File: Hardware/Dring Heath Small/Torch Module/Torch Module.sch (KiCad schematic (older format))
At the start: 32 parts, among them J1 Torch, J10 Module conn, J2 Module3, J3 Conn_01x18_Male, J4 Limit, J6 Motor, J7 Module1, J8 Torch, J9 2.54 pin, K1 G6E, Q1 AO3400A, U1 ULN2002

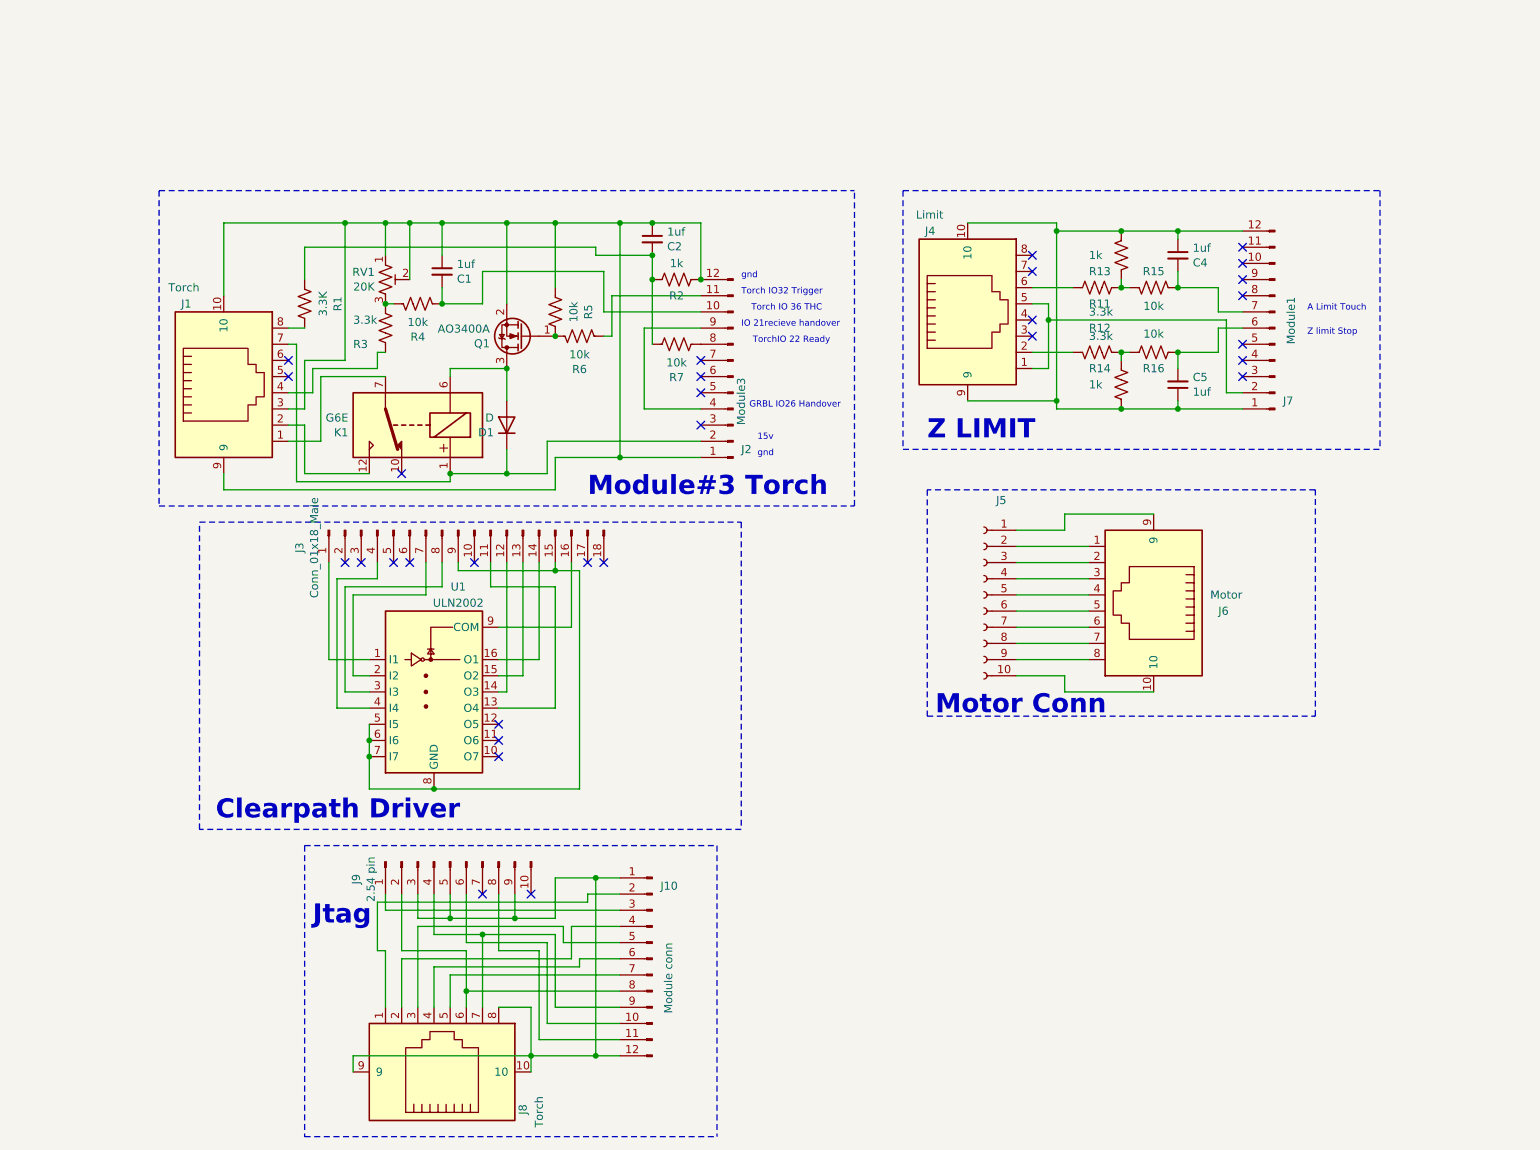
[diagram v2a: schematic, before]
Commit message: Made workspace for vscode
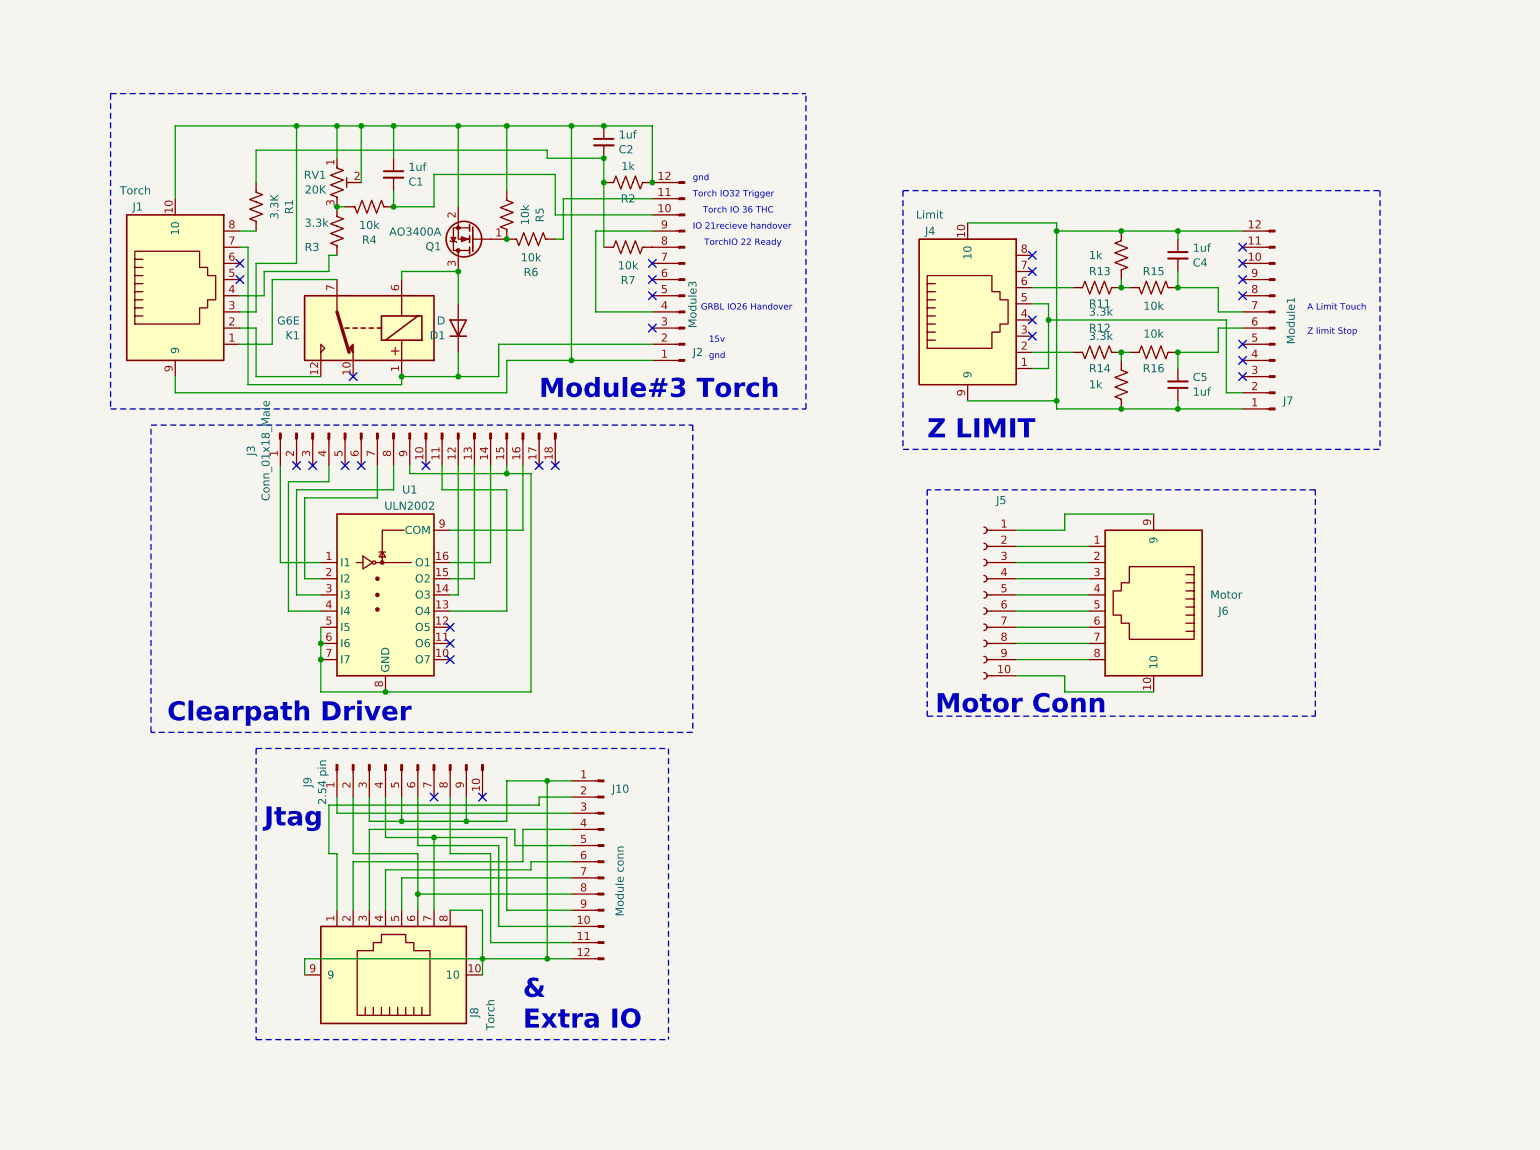
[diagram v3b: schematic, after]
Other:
- note added: "&\nExtra IO"
- moved on the sheet: C1, C2, D1, J1, J10, J2, J3, J8, J9, K1, Q1, R1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

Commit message: Added mosfet motor driver
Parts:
- added J11: Conn_01x18_Male, Modules:ClearpathDriver, symbol Connector:Conn_01x18_Male
- added Q2, Q3, Q4, Q5: IRLML2402, Package_TO_SOT_SMD:SOT-23, symbol Device:Q_NMOS_GDS
- added R10, R18, R20, R8: 200, Resistor_SMD:R_0603_1608Metric_Pad0.98x0.95mm_HandSolder, symbol Device:R_US
- added R17, R19, R21, R9: 10k, Resistor_SMD:R_0603_1608Metric_Pad0.98x0.95mm_HandSolder, symbol Device:R_US
- Q1: value AO3400A -> IRLML2402
- R6: value 10k -> 200
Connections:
- new net: J11.1 (Pin_1), R8.1
- new net: J11.11 (Pin_11), Q5.2 (D)
- new net: J11.12 (Pin_12), Q3.2 (D)
- new net: J11.13 (Pin_13), Q4.2 (D)
- new net: J11.14 (Pin_14), Q2.2 (D)
- new net: J11.15 (Pin_15), J11.9 (Pin_9), Q2.3 (S), Q3.3 (S), Q4.3 (S), Q5.3 (S), R17.2, R19.2, R21.2, R9.2
- new net: J11.4 (Pin_4), R20.1
- new net: J11.7 (Pin_7), R18.1
- new net: J11.8 (Pin_8), R10.1
- new net: Q2.1 (G), R8.2, R9.1
- new net: Q4.1 (G), R18.2, R19.1
- new net: Q3.1 (G), R10.2, R17.1
- new net: Q5.1 (G), R20.2, R21.1
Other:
- note added: "Mosfet Driver"
- moved on the sheet: C1, C2, C4, C5, D1, J1, J10, J2, J3, J4, J5, J6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

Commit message: Changed voltage divider for THC input
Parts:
- C1: value 1uf -> 22nf
- R3: value 3.3k -> 1k
- RV1: value 20K -> 2K
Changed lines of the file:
@@
 AR Path="/61469ABE/61A6725D" Ref="C?"  Part="1"
 F 0 "C1" H 3758 1254 50  0000 R CNN
-F 1 "1uf" H 3758 1345 50  0000 R CNN
+F 1 "22nf" H 3758 1345 50  0000 R CNN
 F 2 "Capacitor_SMD:C_0603_1608Metric_Pad1.08x0.95mm_HandSolder" H 3850 1300 50  0001 C CNN
 F 3 "~" H 3850 1300 50  0001 C CNN
@@
 AR Path="/61469ABE/61A6724B" Ref="R?"  Part="1"
 F 0 "R3" H 3700 1750 50  0000 R CNN
-F 1 "3.3k" H 3700 1600 50  0000 R CNN
+F 1 "1k" H 3700 1600 50  0000 R CNN
 F 2 "Resistor_SMD:R_0603_1608Metric_Pad0.98x0.95mm_HandSolder" V 3540 1640 50  0001 C CNN
 F 3 "~" H 3500 1650 50  0001 C CNN
@@
 P 3500 1350
 F 0 "RV1" H 3433 1396 50  0000 R CNN
-F 1 "20K" H 3433 1305 50  0000 R CNN
+F 1 "2K" H 3433 1305 50  0000 R CNN
 F 2 "Potentiometer_THT:Potentiometer_Bourns_3339S_Horizontal" H 3500 1350 50  0001 C CNN
 F 3 "~" H 3500 1350 50  0001 C CNN

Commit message: put protection resistors on JTAG module
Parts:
- added R22, R23, R24, R25, R26, R27, R28, R29: 200, Resistor_SMD:R_0603_1608Metric_Pad0.98x0.95mm_HandSolder, symbol Device:R_US
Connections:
- net at J10.10 (Pin_10): now also R28.1; no longer J9.6 (Pin_6)
- net at J10.11 (Pin_11): now also R29.1; no longer J9.8 (Pin_8)
- net at J10.4 (Pin_4): now also R22.1; no longer J8.2
- net at J10.5 (Pin_5): now also R23.1; no longer J8.3
- net at J10.6 (Pin_6): now also R24.1; no longer J8.4
- net at J10.7 (Pin_7): now also R25.1; no longer J8.5
- net at J8.6, J9.2 (Pin_2): now also R26.2; no longer J10.8 (Pin_8)
- net at J8.7, J9.4 (Pin_4): now also R27.2; no longer J10.9 (Pin_9)
- new net: J10.8 (Pin_8), R26.1
- new net: J10.9 (Pin_9), R27.1
- new net: J9.6 (Pin_6), R28.2
- new net: J9.8 (Pin_8), R29.2
- new net: J8.2, R22.2
- new net: J8.3, R23.2
- new net: J8.4, R24.2
- new net: J8.5, R25.2
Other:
- moved on the sheet: J10
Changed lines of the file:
@@
 	3500 5150 3500 5250
 Wire Wire Line
-	3500 5250 4950 5250
+	3500 5250 5150 5250
 Wire Wire Line
 	4600 5350 4600 5450
 Wire Wire Line
-	4600 5450 4950 5450
-Wire Wire Line
 	4550 5300 4550 5050
 Wire Wire Line
-	4550 5050 4800 5050
-Wire Wire Line
 	3800 5150 3800 5400
 Wire Wire Line
@@
 	4550 5400 4550 5850
 Wire Wire Line
-	4550 5850 4950 5850
-Wire Wire Line
 	4000 5150 4000 5450
 Wire Wire Line
@@
 	4500 5450 4500 5950
 Wire Wire Line
-	4500 5950 4950 5950
-Wire Wire Line
 	4200 5150 4200 5500
 Wire Wire Line
@@
 	4450 5500 4450 6050
 Wire Wire Line
-	4450 6050 4950 6050
-Wire Wire Line
 	4400 6250 4400 6150
-Wire Wire Line
-	4400 6150 4800 6150
 Wire Wire Line
 	4750 5200 3450 5200
@@
 L Connector:Conn_01x12_Male J?
 U 1 1 600F49D0
-P 5150 5550
+P 5350 5550
 AR Path="/61469ABE/600F49D0" Ref="J?"  Part="1"
 AR Path="/600F49D0" Ref="J10"  Part="1"
-F 0 "J10" H 5100 6000 50  0000 R CNN
-F 1 "Module conn" V 5050 5650 50  0000 R CNN
-F 2 "Connector_PinHeader_2.54mm:PinHeader_1x12_P2.54mm_Vertical" H 5150 5550 50  0001 C CNN
-F 3 "~" H 5150 5550 50  0001 C CNN
-	1    5150 5550
+F 0 "J10" H 5300 6000 50  0000 R CNN
+F 1 "Module conn" V 5250 5650 50  0000 R CNN
+F 2 "Connector_PinHeader_2.54mm:PinHeader_1x12_P2.54mm_Vertical" H 5350 5550 50  0001 C CNN
+F 3 "~" H 5350 5550 50  0001 C CNN
+	1    5350 5550
 	-1   0    0    -1
 $EndComp
@@
 	4750 5200 4750 5150
 Wire Wire Line
-	4750 5150 4950 5150
-Wire Wire Line
-	4950 5350 4650 5350
+	4750 5150 5150 5150
 Wire Wire Line
 	4650 5350 4650 5550
@@
 	3700 5350 3700 5850
 Wire Wire Line
-	4950 5550 4700 5550
-Wire Wire Line
 	4700 5550 4700 5600
 Wire Wire Line
@@
 	3800 5600 3800 5850
 Wire Wire Line
-	4950 5650 3900 5650
-Wire Wire Line
 	3900 5650 3900 5850
-Wire Wire Line
-	4950 5750 4000 5750
-Wire Wire Line
-	4000 5750 4000 5850
 Wire Wire Line
 	4100 5400 4100 5850
@@
 NoConn ~ 4400 5150
 NoConn ~ 4100 5150
-Wire Wire Line
-	4800 6150 4800 5050
-Connection ~ 4800 6150
-Wire Wire Line
-	4800 6150 4950 6150
-Connection ~ 4800 5050
-Wire Wire Line
-	4800 5050 4950 5050
 Wire Notes Line
 	2100 800  6400 800
@@
 Connection ~ 4300 5300
 Wire Wire Line
-	4300 5300 4550 5300
+	4300 5300 4400 5300
 Wire Wire Line
 	3900 5150 3900 5300
@@
 	3700 5300 3900 5300
 Wire Wire Line
-	4000 5750 4000 5500
-Wire Wire Line
 	4000 5500 3600 5500
 Wire Wire Line
 	3600 5150 3600 5500
-Connection ~ 4000 5750
 Text Notes 4650 6600 0    118  ~ 24
    &\nExtra IO
@@
 Text Notes 8250 4200 0    118  ~ 0
 Mosfet Driver
+$Comp
+L Device:R_US R22
+U 1 1 601AD939
+P 5000 5350
+AR Path="/601AD939" Ref="R22"  Part="1"
+AR Path="/61469ABE/601AD939" Ref="R?"  Part="1"
+F 0 "R22" V 4950 5450 50  0000 C CNN
+F 1 "200" V 4950 5150 50  0000 C CNN
+F 2 "Resistor_SMD:R_0603_1608Metric_Pad0.98x0.95mm_HandSolder" V 5040 5340 50  0001 C CNN
+F 3 "~" H 5000 5350 50  0001 C CNN
+	1    5000 5350
+	0    1    1    0
+$EndComp
+Wire Wire Line
+	4400 6150 5150 6150
+Wire Wire Line
+	4550 5050 5150 5050
+Wire Wire Line
+	4400 5850 4400 5300
+Connection ~ 4400 5850
+Connection ~ 4400 5300
+Wire Wire Line
+	4400 5300 4550 5300
+Wire Wire Line
+	4000 5500 4000 5750
+$Comp
+L Device:R_US R23
+U 1 1 601E3A12
+P 5000 5450
+AR Path="/601E3A12" Ref="R23"  Part="1"
+AR Path="/61469ABE/601E3A12" Ref="R?"  Part="1"
+F 0 "R23" V 4950 5550 50  0000 C CNN
+F 1 "200" V 4950 5250 50  0000 C CNN
+F 2 "Resistor_SMD:R_0603_1608Metric_Pad0.98x0.95mm_HandSolder" V 5040 5440 50  0001 C CNN
+F 3 "~" H 5000 5450 50  0001 C CNN
+	1    5000 5450
+	0    1    1    0
+$EndComp
+$Comp
+L Device:R_US R24
+U 1 1 601E46FB
+P 5000 5550
+AR Path="/601E46FB" Ref="R24"  Part="1"
+AR Path="/61469ABE/601E46FB" Ref="R?"  Part="1"
+F 0 "R24" V 4950 5650 50  0000 C CNN
+F 1 "200" V 4950 5350 50  0000 C CNN
+F 2 "Resistor_SMD:R_0603_1608Metric_Pad0.98x0.95mm_HandSolder" V 5040 5540 50  0001 C CNN
+F 3 "~" H 5000 5550 50  0001 C CNN
+	1    5000 5550
+	0    1    1    0
+$EndComp
+$Comp
+L Device:R_US R25
+U 1 1 601E5E3A
+P 5000 5650
+AR Path="/601E5E3A" Ref="R25"  Part="1"
+AR Path="/61469ABE/601E5E3A" Ref="R?"  Part="1"
+F 0 "R25" V 4950 5750 50  0000 C CNN
+F 1 "200" V 4950 5450 50  0000 C CNN
+F 2 "Resistor_SMD:R_0603_1608Metric_Pad0.98x0.95mm_HandSolder" V 5040 5640 50  0001 C CNN
+F 3 "~" H 5000 5650 50  0001 C CNN
+	1    5000 5650
+	0    1    1    0
+$EndComp
+$Comp
+L Device:R_US R26
+U 1 1 601E6C26
+P 5000 5750
+AR Path="/601E6C26" Ref="R26"  Part="1"
+AR Path="/61469ABE/601E6C26" Ref="R?"  Part="1"
+F 0 "R26" V 4950 5850 50  0000 C CNN
+F 1 "200" V 4950 5550 50  0000 C CNN
+F 2 "Resistor_SMD:R_0603_1608Metric_Pad0.98x0.95mm_HandSolder" V 5040 5740 50  0001 C CNN
+F 3 "~" H 5000 5750 50  0001 C CNN
+	1    5000 5750
+	0    1    1    0
+$EndComp
+$Comp
+L Device:R_US R27
+U 1 1 601E79D9
+P 5000 5850
+AR Path="/601E79D9" Ref="R27"  Part="1"
+AR Path="/61469ABE/601E79D9" Ref="R?"  Part="1"
+F 0 "R27" V 4950 5950 50  0000 C CNN
+F 1 "200" V 4950 5650 50  0000 C CNN
+F 2 "Resistor_SMD:R_0603_1608Metric_Pad0.98x0.95mm_HandSolder" V 5040 5840 50  0001 C CNN
+F 3 "~" H 5000 5850 50  0001 C CNN
+	1    5000 5850
+	0    1    1    0
+$EndComp
+$Comp
+L Device:R_US R28
+U 1 1 601E891C
+P 5000 5950
+AR Path="/601E891C" Ref="R28"  Part="1"
+AR Path="/61469ABE/601E891C" Ref="R?"  Part="1"
+F 0 "R28" V 4950 6050 50  0000 C CNN
+F 1 "200" V 4950 5750 50  0000 C CNN
+F 2 "Resistor_SMD:R_0603_1608Metric_Pad0.98x0.95mm_HandSolder" V 5040 5940 50  0001 C CNN
+F 3 "~" H 5000 5950 50  0001 C CNN
+	1    5000 5950
+	0    1    1    0
+$EndComp
+$Comp
+L Device:R_US R29
+U 1 1 601EAB04
+P 5000 6050
+AR Path="/601EAB04" Ref="R29"  Part="1"
+AR Path="/61469ABE/601EAB04" Ref="R?"  Part="1"
+F 0 "R29" V 4950 6150 50  0000 C CNN
+F 1 "200" V 4950 5850 50  0000 C CNN
+F 2 "Resistor_SMD:R_0603_1608Metric_Pad0.98x0.95mm_HandSolder" V 5040 6040 50  0001 C CNN
+F 3 "~" H 5000 6050 50  0001 C CNN
+	1    5000 6050
+	0    1    1    0
+$EndComp
+Wire Wire Line
+	4450 6050 4850 6050
+Wire Wire Line
+	4500 5950 4850 5950
+Wire Wire Line
+	4550 5850 4850 5850
+Wire Wire Line
+	4700 5550 4850 5550
+Wire Wire Line
+	4600 5450 4850 5450
+Wire Wire Line
+	4650 5350 4850 5350
+Wire Wire Line
+	3900 5650 4850 5650
+Wire Wire Line
+	4850 5750 4000 5750
+Connection ~ 4000 5750
+Wire Wire Line
+	4000 5750 4000 5850
 $EndSCHEMATC

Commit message: fixed voltage divider for THC
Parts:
- C1: value 22nf -> 100nf
- R3: value 1k -> 3.3K
- R7: value 10k -> 200
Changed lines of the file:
@@
 AR Path="/61469ABE/61A6725D" Ref="C?"  Part="1"
 F 0 "C1" H 3758 1254 50  0000 R CNN
-F 1 "22nf" H 3758 1345 50  0000 R CNN
+F 1 "100nf" H 3758 1345 50  0000 R CNN
 F 2 "Capacitor_SMD:C_0603_1608Metric_Pad1.08x0.95mm_HandSolder" H 3850 1300 50  0001 C CNN
 F 3 "~" H 3850 1300 50  0001 C CNN
@@
 AR Path="/61469ABE/61A6724B" Ref="R?"  Part="1"
 F 0 "R3" H 3700 1750 50  0000 R CNN
-F 1 "1k" H 3700 1600 50  0000 R CNN
+F 1 "3.3K" H 3700 1600 50  0000 R CNN
 F 2 "Resistor_SMD:R_0603_1608Metric_Pad0.98x0.95mm_HandSolder" V 3540 1640 50  0001 C CNN
 F 3 "~" H 3500 1650 50  0001 C CNN
@@
 AR Path="/61469ABE/601384CF" Ref="R?"  Part="1"
 F 0 "R7" V 5095 1750 50  0000 C CNN
-F 1 "10k" V 5186 1750 50  0000 C CNN
+F 1 "200" V 5186 1750 50  0000 C CNN
 F 2 "Resistor_SMD:R_0603_1608Metric_Pad0.98x0.95mm_HandSolder" V 5340 1740 50  0001 C CNN
 F 3 "~" H 5300 1750 50  0001 C CNN
